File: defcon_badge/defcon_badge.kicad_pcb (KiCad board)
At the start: 4 copper layers, 89 x 54 mm, 80 parts, among them J10 USB_C_Receptacle_GCT_USB4085, J11 JST-PH 2P, J20 AMPHENOL_10038075-D0P, J30 SAO 2x3, J31 microSD, J32 UART debug, J33 Dev/SWD header, SW1 SS-12D00, SW20 TS-1187A, SW21 TS-1187A, SW22 TS-1187A, U10 TP4056, U11 ME6211C33M5G, U2 W25Q16JVUXIQ, U20 TM8211, U21 TDA1308, U3 RP2040, U30 TSOP4838, Y1 ABM8-272-T3

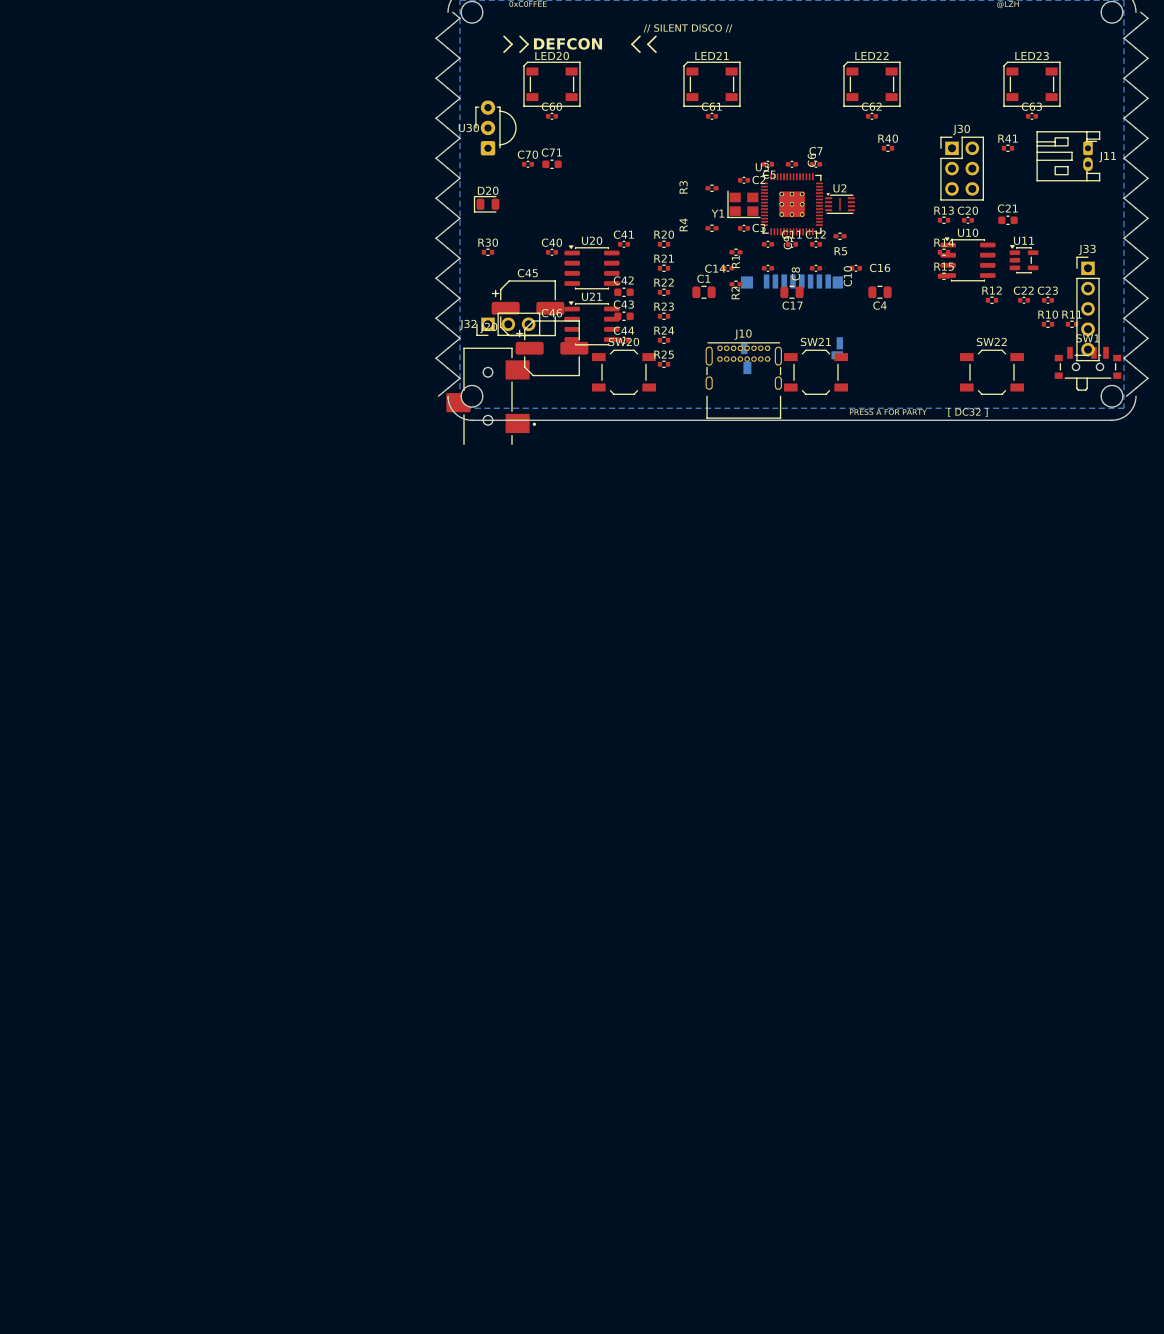
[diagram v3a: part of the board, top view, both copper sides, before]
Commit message: iter(31): depopulate — sweep all components to staging grid below board
New tools/sweep_offboard.py moves every non-mounting-hole footprint
to a staging grid at (50, 200) with 10mm column / 8mm row pitch.
Board is now empty (just the sawtooth outline + 4 corner mounting
holes) and ready for a deliberate re-placement pass.

Co-Authored-By: Claude Opus 4.7 (1M context) <noreply@anthropic.com>
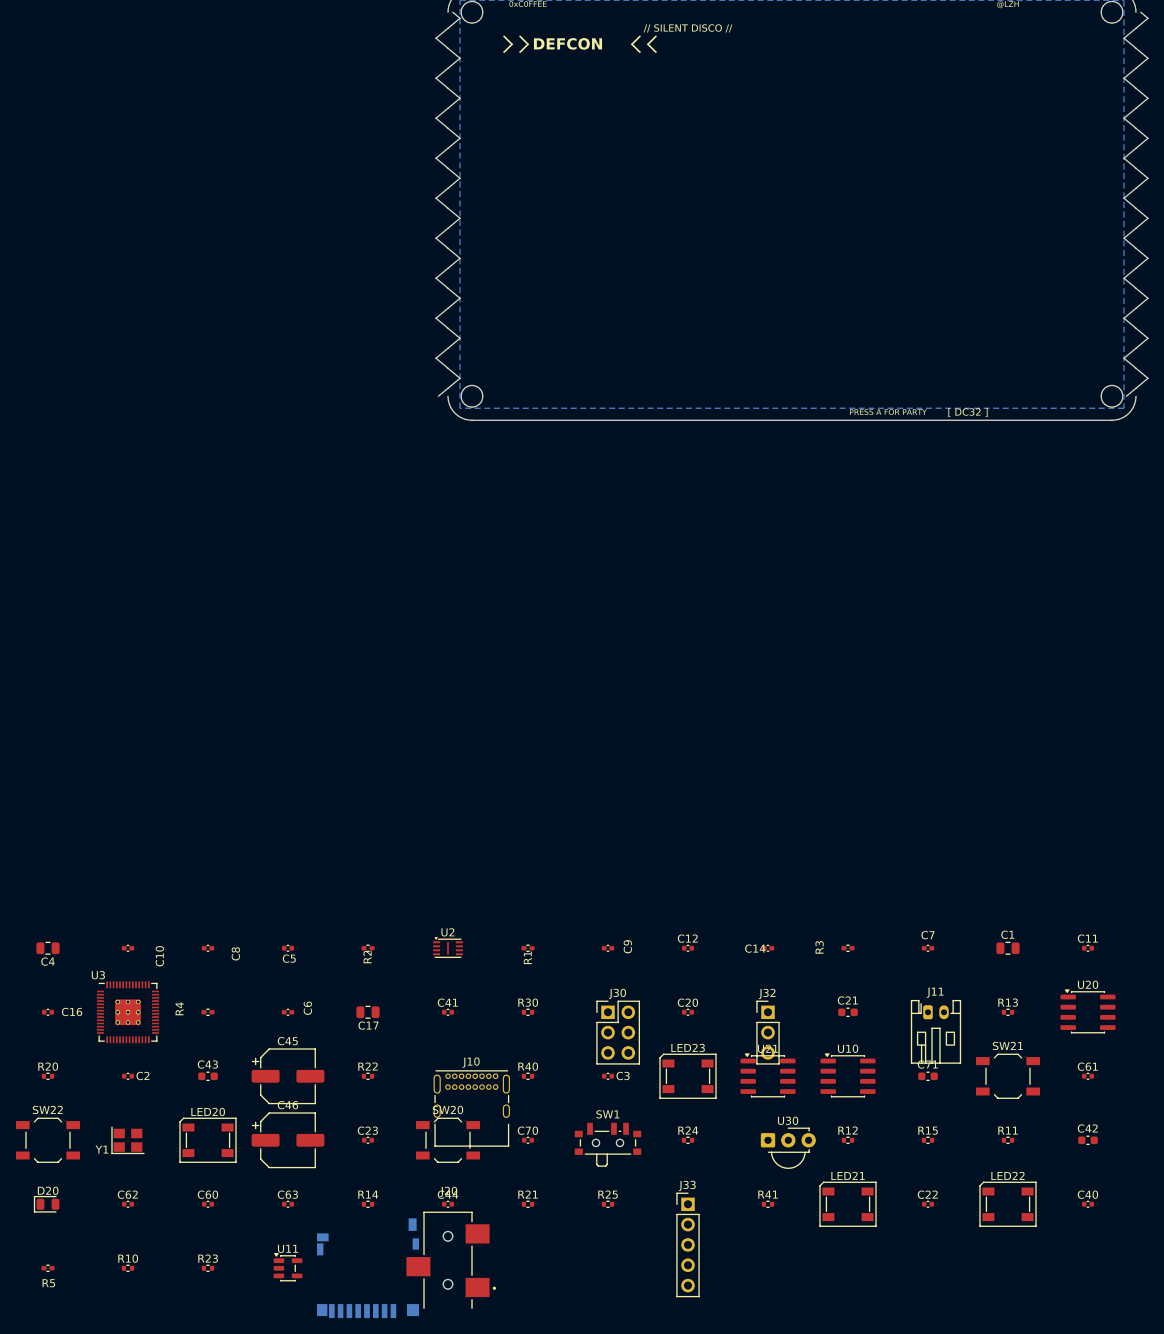
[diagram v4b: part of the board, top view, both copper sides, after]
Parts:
- moved R10 164.8 mm to (60.0, 240.0)
- moved C62 164.8 mm to (60.0, 232.0)
- moved C63 164.8 mm to (80.0, 232.0)
- moved R5 162.6 mm to (50.0, 240.0)
- moved U11 156.0 mm to (80.0, 240.0)
- moved SW22 152.1 mm to (50.0, 224.0)
- moved C60 142.6 mm to (70.0, 232.0)
- moved LED21 141.0 mm to (150.0, 232.0)
- moved LED22 141.0 mm to (170.0, 232.0)
- moved Y1 140.1 mm to (60.0, 224.0)
- moved R14 139.1 mm to (90.0, 232.0)
- moved LED20 138.8 mm to (70.0, 224.0)
- moved C16 137.3 mm to (50.0, 208.0)
- moved D20 136.6 mm to (50.0, 232.0)
- moved C40 136.6 mm to (180.0, 232.0)
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
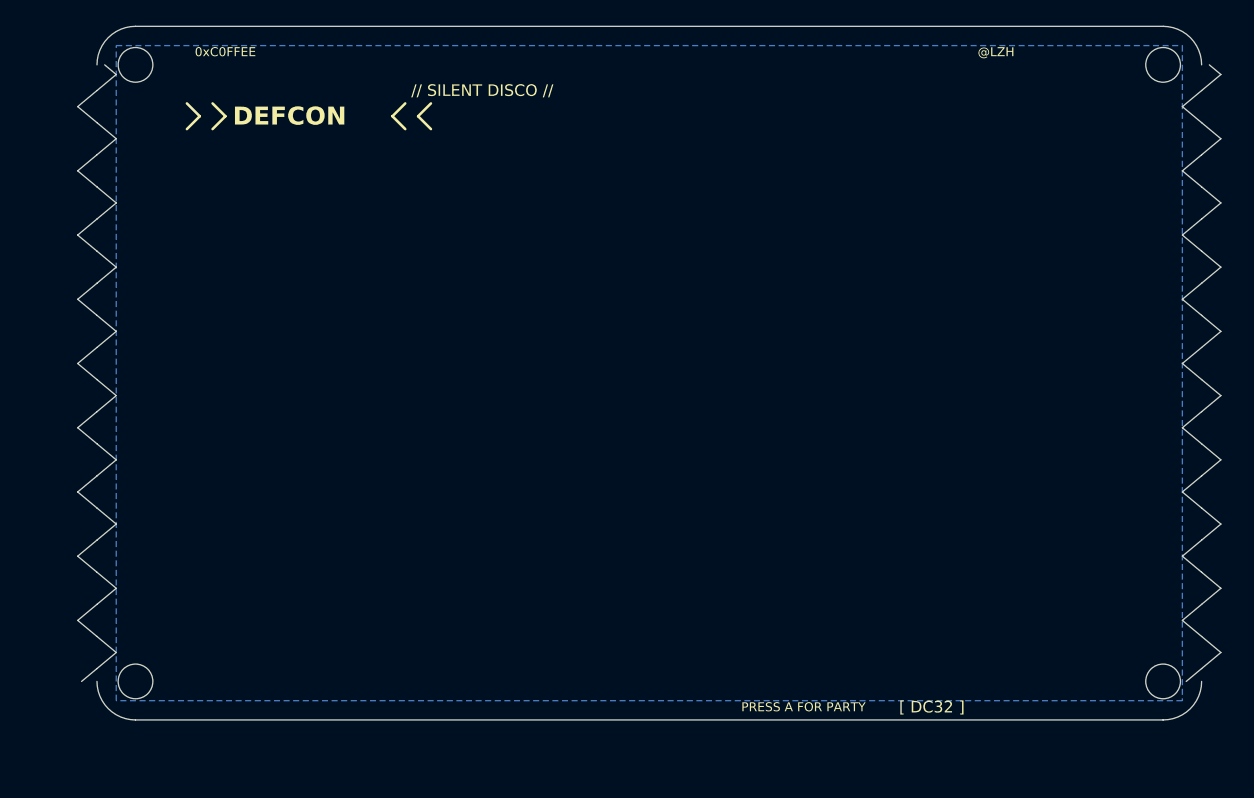
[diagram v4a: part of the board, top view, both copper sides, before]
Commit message: iter(30 redo): real sawtooth — long ramp + sharp drop, both edges, mating
set_outline_v2.py was generating a triangle wave (symmetric peaks).
Rewritten as a true sawtooth — long ramp up, sharp drop back to baseline.

  Right edge: teeth (peaks point +X, sticking out from board)
  Left edge:  same polyline shape (notches that point +X, into board)
  When two boards meet edge-to-edge, A's right teeth occupy the same
  world position as B's left notches → boards mate.

Other fixes this iteration:
- All four corners are now SHARP (no rounding). Rounded corners would
  leave a triangular gap at the meeting edges.
- Strip Edge.Cuts properly via balanced-paren walk (the old inline
  rectangle was being left behind, so geometry was duplicated).
- drop_frac=0.85 so ramp takes 85% of period, drop takes 15%. Avoids
  zero-area horizontal segments that confused the 3D renderer.
- T=6mm, depth=2mm, 9 teeth per side, board 86x54mm.
- IR alignment Y=110 picked to land on a right-peak / left-notch pair
  so D20 and U30 face each other across the gap when boards mate.

Co-Authored-By: Claude Opus 4.7 (1M context) <noreply@anthropic.com>
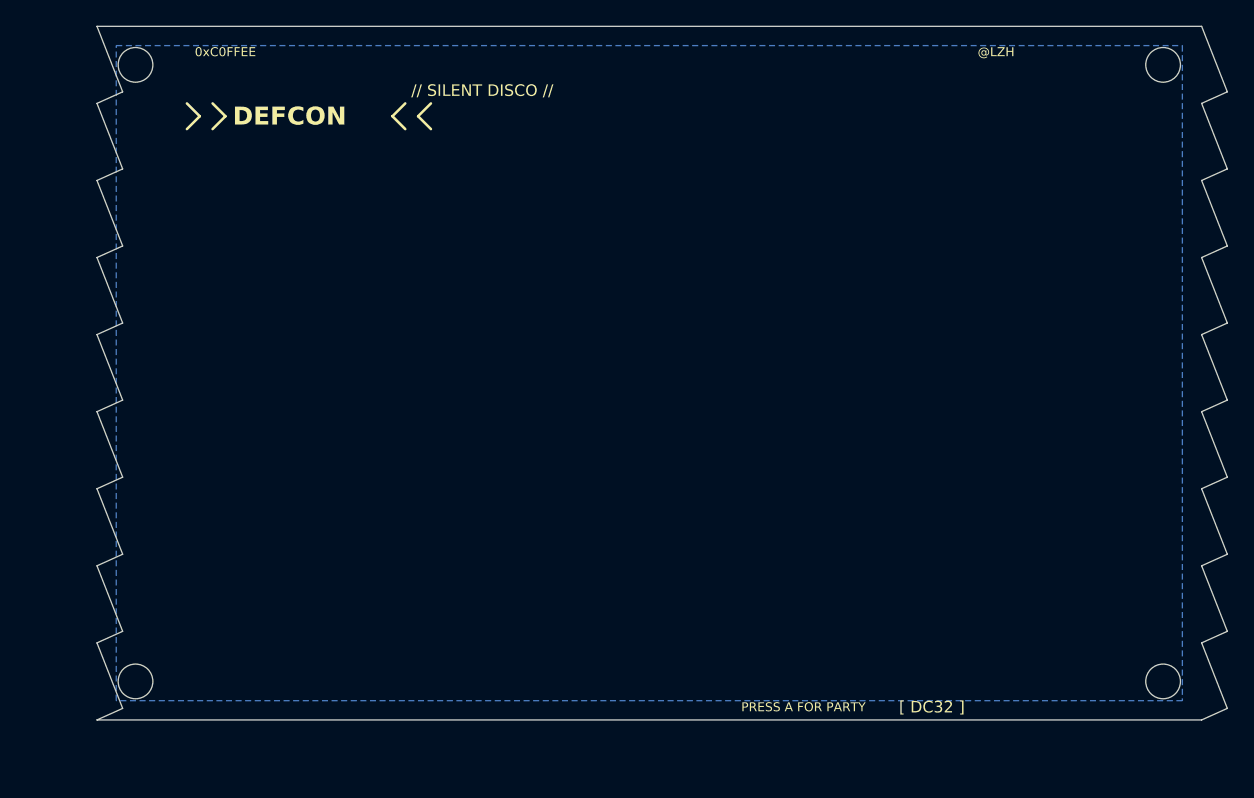
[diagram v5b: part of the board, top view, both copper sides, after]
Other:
- board size 89 x 54 mm -> 88 x 54 mm

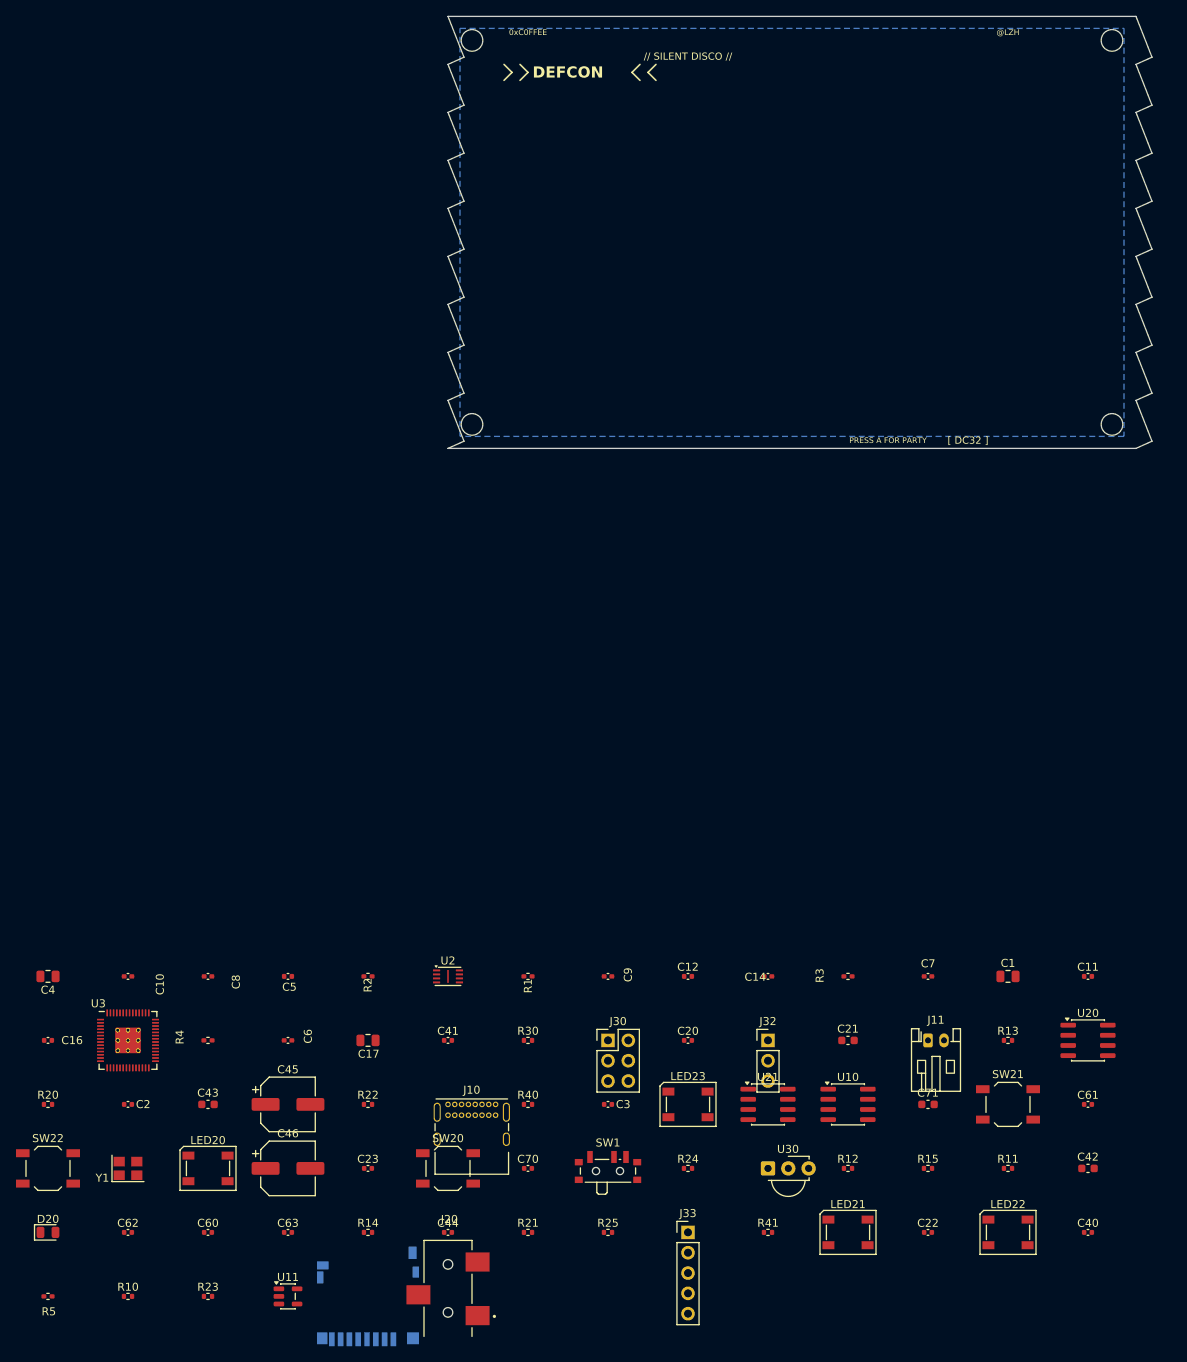
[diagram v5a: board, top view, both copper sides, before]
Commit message: iter(31-32): re-populate board with new floor plan
Floor plan per user constraints:
- TOP: LED row (LED20-23) + LED bypass caps + audio block (U20 DAC,
  U21 amp, C40-C46 caps, R20-R25)
- LEFT edge (sawtooth notches): U30 IR receiver @ y=110, audio jack J20
  body off-board, SAO header J30, UART J32
- RIGHT edge (sawtooth peaks): D20 IR LED @ y=110, J11 battery body
  off-edge, SW1 power slide switch, R30 IR current limit
- CENTER: MCU cluster (U3 RP2040 + Y1 + U2 + decoupling ring)
- INTERIOR: 3 push buttons SW20-22 mid-board (per user request)
- BOTTOM: USB-C J10 body off-bottom, charger (U10 TP4056) + LDO (U11
  ME6211) + caps/resistors, SWD J33, UART moved here
- BACK: microSD J31 flipped via flip_footprint.py to clear front-side
  real estate near USB-C

check_courtyards.py updated to skip F.Cu/B.Cu pairs (they can't physically
collide). Currently 14 overlaps remaining, mostly small (<2mm²) and in
the dense MCU decoupling ring (intentional close coupling) — 4-5 remain
to fix in the next pass: J20↔H3 corner, U21↔C46 audio caps spacing,
buttons↔neighbors.

Co-Authored-By: Claude Opus 4.7 (1M context) <noreply@anthropic.com>
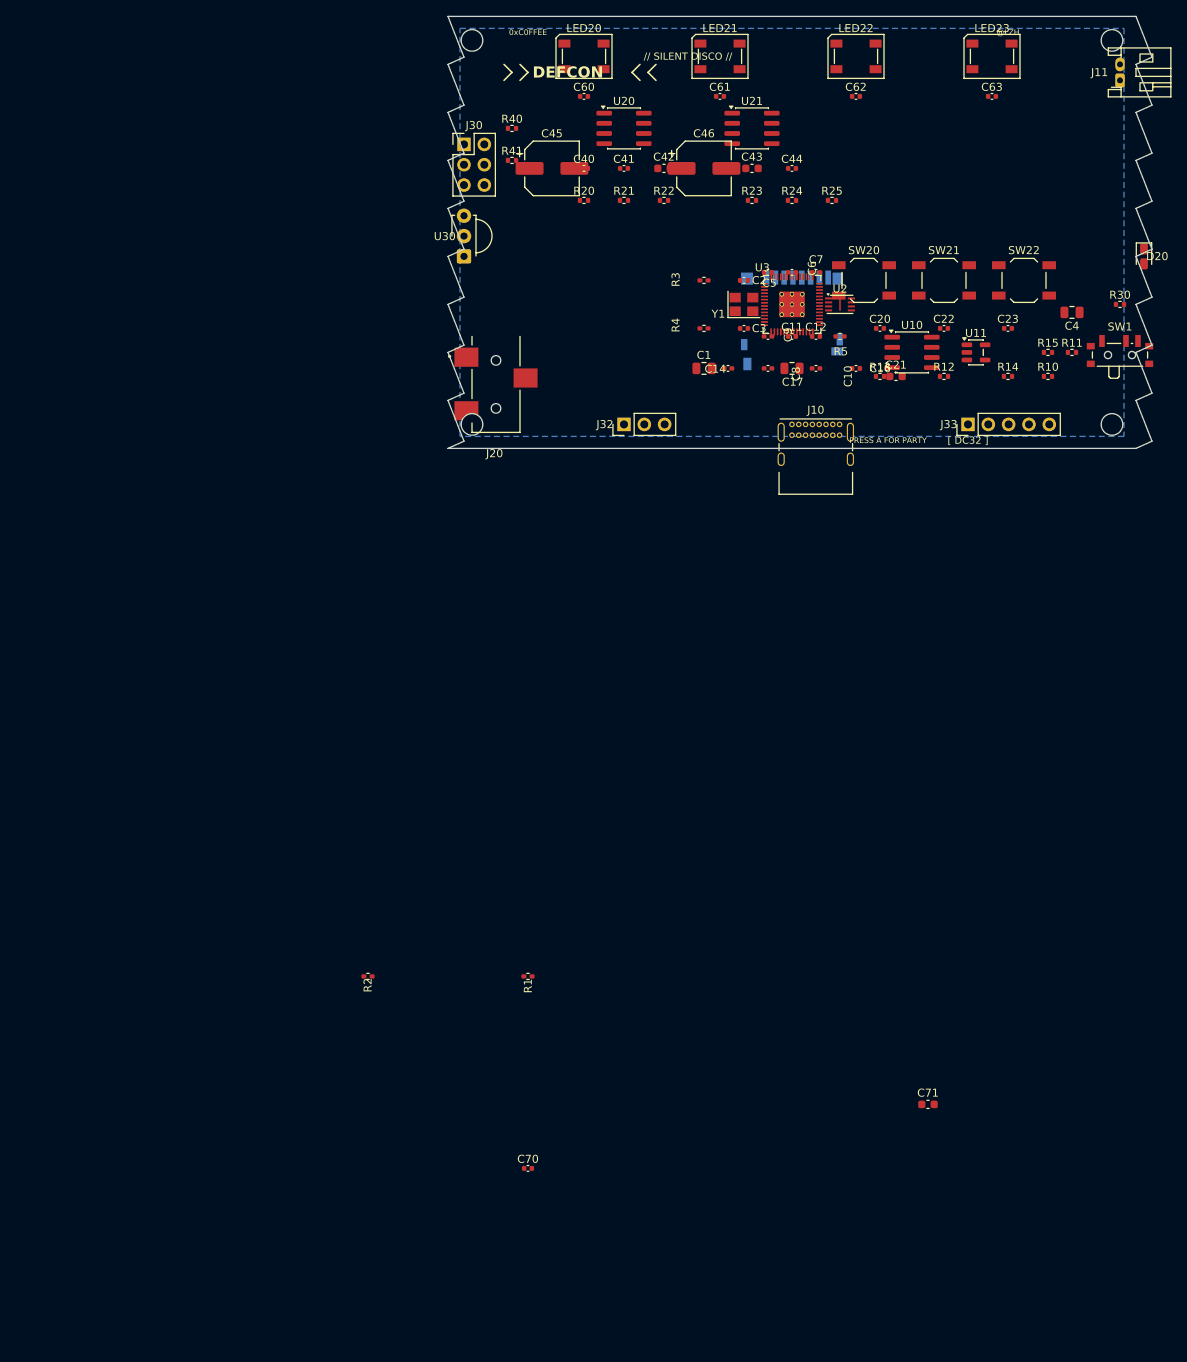
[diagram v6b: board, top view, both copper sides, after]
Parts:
- moved D20 183.4 mm to (187.0, 110.0), turned to 270 degrees
- moved C62 168.7 mm to (151.0, 90.0)
- moved C63 167.1 mm to (168.0, 90.0)
- moved SW22 164.9 mm to (172.0, 113.0)
- moved R10 162.6 mm to (175.0, 125.0)
- moved R5 155.6 mm to (149.0, 120.0)
- moved R23 152.9 mm to (138.0, 103.0)
- moved C4 152.6 mm to (178.0, 117.0)
- moved C60 149.6 mm to (117.0, 90.0)
- moved LED22 148.2 mm to (151.0, 85.0)
- moved LED21 147.9 mm to (134.0, 85.0)
- moved C40 147.2 mm to (117.0, 99.0)
- moved LED20 146.7 mm to (117.0, 85.0)
- moved U11 146.0 mm to (166.0, 122.0)
- moved C44 139.8 mm to (143.0, 99.0)
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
